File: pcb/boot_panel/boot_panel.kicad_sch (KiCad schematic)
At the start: 4 parts, among them J1 Conn_01x10_Socket

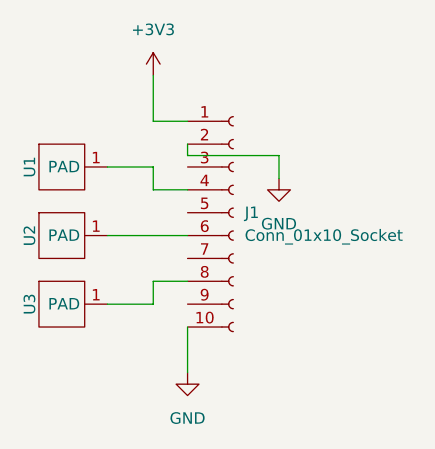
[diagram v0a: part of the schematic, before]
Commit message: move panel connector to fpc
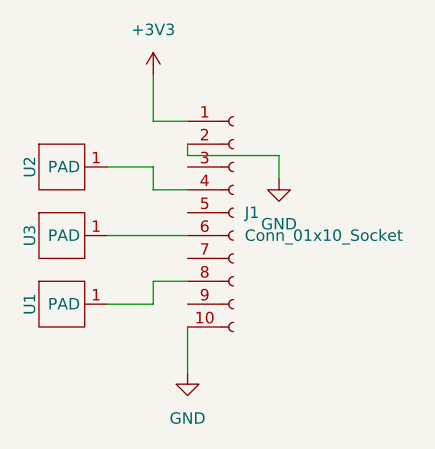
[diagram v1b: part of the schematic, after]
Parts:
- J1: footprint Connector_PinHeader_2.54mm:PinHeader_1x10_P2.54mm_Vertical_SMD_Pin1Left -> Connector_FFC-FPC:Hirose_FH12-10S-0.5SH_1x10-1MP_P0.50mm_Horizontal
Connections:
- net at U2.1 (PAD): now also J1.4 (Pin_4); no longer J1.6 (Pin_6)
- net at U1.1 (PAD): now also J1.8 (Pin_8); no longer J1.4 (Pin_4)
- net at U3.1 (PAD): now also J1.6 (Pin_6); no longer J1.8 (Pin_8)
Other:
- moved on the sheet: U1, U2, U3
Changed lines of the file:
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@@
 	(symbol
 		(lib_id "cap_pads:capacitive_pad")
-		(at 175.26 81.28 0)
+		(at 175.26 73.66 0)
 		(unit 1)
 		(exclude_from_sim no)
@@
 		(dnp no)
 		(property "Reference" "U2"
-			(at 171.704 85.09 90)
+			(at 171.704 77.47 90)
 			(effects
 				(font
@@
 		)
 		(property "Value" "~"
-			(at 175.26 81.28 0)
+			(at 175.26 73.66 0)
 			(effects
 				(font
@@
 		)
 		(property "Footprint" "cap_pads:square_20x20mm"
-			(at 175.26 81.28 0)
+			(at 175.26 73.66 0)
 			(effects
 				(font
@@
 		)
 		(property "Datasheet" ""
-			(at 175.26 81.28 0)
+			(at 175.26 73.66 0)
 			(effects
 				(font
@@
 		)
 		(property "Description" ""
-			(at 175.26 81.28 0)
+			(at 175.26 73.66 0)
 			(effects
 				(font
@@
 			)
 		)
-		(property "Footprint" "Connector_PinHeader_2.54mm:PinHeader_1x10_P2.54mm_Vertical_SMD_Pin1Left"
+		(property "Footprint" "Connector_FFC-FPC:Hirose_FH12-10S-0.5SH_1x10-1MP_P0.50mm_Horizontal"
 			(at 194.31 82.55 0)
 			(effects
@@
 	(symbol
 		(lib_id "cap_pads:capacitive_pad")
-		(at 175.26 88.9 0)
+		(at 175.26 81.28 0)
 		(unit 1)
 		(exclude_from_sim no)
@@
 		(dnp no)
 		(property "Reference" "U3"
-			(at 171.704 92.71 90)
+			(at 171.704 85.09 90)
 			(effects
 				(font
@@
 		)
 		(property "Value" "~"
-			(at 175.26 88.9 0)
+			(at 175.26 81.28 0)
 			(effects
 				(font
@@
 		)
 		(property "Footprint" "cap_pads:square_20x20mm"
-			(at 175.26 88.9 0)
+			(at 175.26 81.28 0)
 			(effects
 				(font
@@
 		)
 		(property "Datasheet" ""
-			(at 175.26 88.9 0)
+			(at 175.26 81.28 0)
 			(effects
 				(font
@@
 		)
 		(property "Description" ""
-			(at 175.26 88.9 0)
+			(at 175.26 81.28 0)
 			(effects
 				(font
@@
 	(symbol
 		(lib_id "cap_pads:capacitive_pad")
-		(at 175.26 73.66 0)
+		(at 175.26 88.9 0)
 		(unit 1)
 		(exclude_from_sim no)
@@
 		(dnp no)
 		(property "Reference" "U1"
-			(at 171.704 77.47 90)
+			(at 171.704 92.71 90)
 			(effects
 				(font
@@
 		)
 		(property "Value" "~"
-			(at 175.26 73.66 0)
+			(at 175.26 88.9 0)
 			(effects
 				(font
@@
 		)
 		(property "Footprint" "cap_pads:square_20x20mm"
-			(at 175.26 73.66 0)
+			(at 175.26 88.9 0)
 			(effects
 				(font
@@
 		)
 		(property "Datasheet" ""
-			(at 175.26 73.66 0)
+			(at 175.26 88.9 0)
 			(effects
 				(font
@@
 		)
 		(property "Description" ""
-			(at 175.26 73.66 0)
-			(effects
-				(font
+			(at 175.26 88.9 0)
+			(effects
+				(font

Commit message: MOre layout
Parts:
- added H1, H2, H3, H4: MountingHole, MountingHole:MountingHole_3.2mm_M3, symbol Mechanical:MountingHole

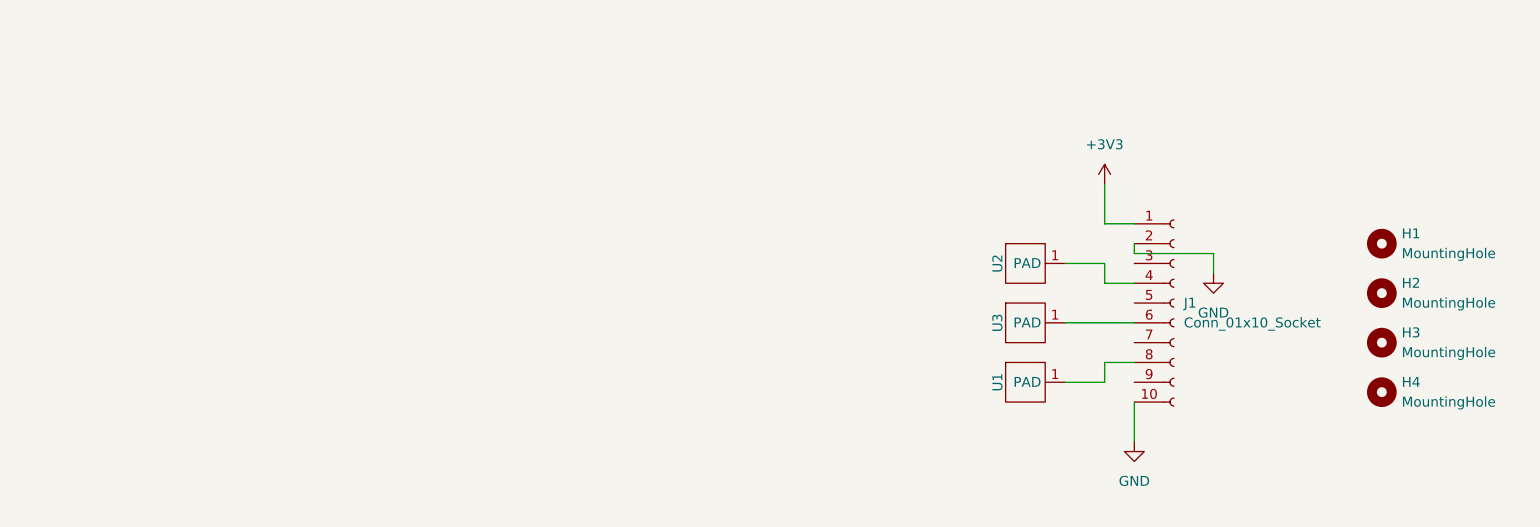
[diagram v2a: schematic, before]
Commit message: move cap sense ic to front panel
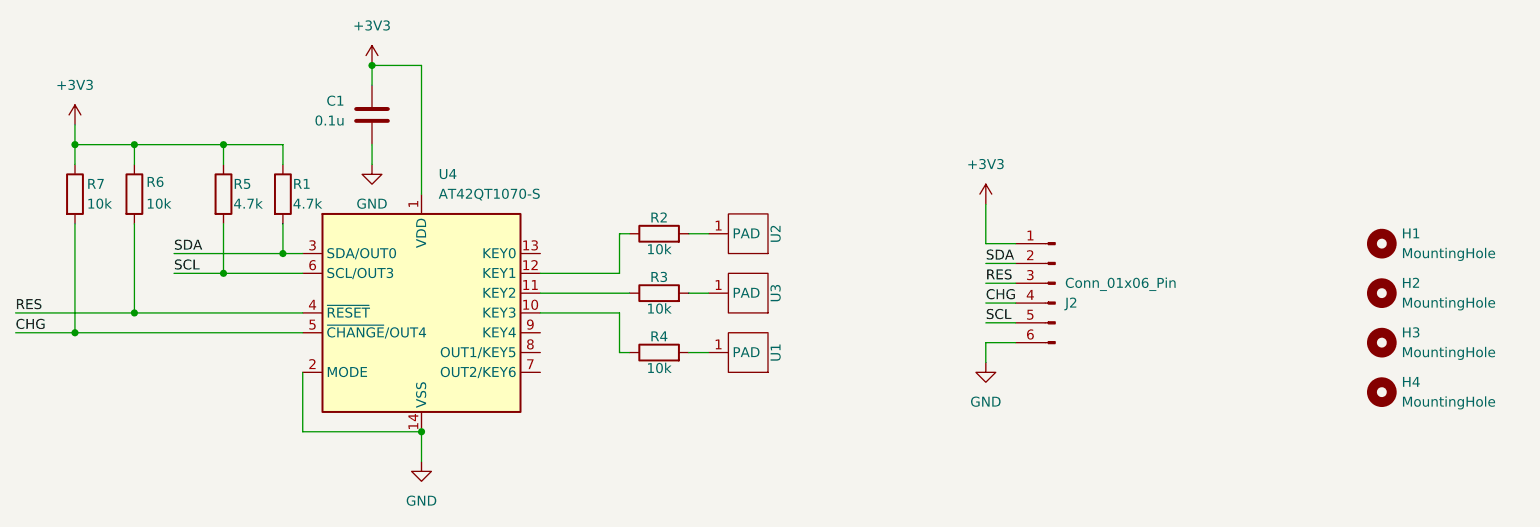
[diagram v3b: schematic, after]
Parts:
- removed J1: Conn_01x10_Socket, Connector_FFC-FPC:Hirose_FH12-10S-0.5SH_1x10-1MP_P0.50mm_Horizontal, symbol Connector:Conn_01x10_Socket
- added C1: 0.1u, Capacitor_SMD:C_0402_1005Metric, symbol Device:C
- added J2: Conn_01x06_Pin, Connector_FFC-FPC:Hirose_FH12-6S-0.5SH_1x06-1MP_P0.50mm_Horizontal, symbol Connector:Conn_01x06_Pin
- added R1, R5: 4.7k, Resistor_SMD:R_0402_1005Metric, symbol Device:R
- added R2, R3, R4, R6, R7: 10k, Resistor_SMD:R_0402_1005Metric, symbol Device:R
- added U4: AT42QT1070-S, Package_SO:SOIC-14_3.9x8.7mm_P1.27mm, symbol Sensor_Touch:AT42QT1070-S
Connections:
- net +3V3: now also C1.1, J2.1 (Pin_1), R1.1, R5.1, R6.1, R7.1, U4.1 (VDD)
- net GND: now also C1.2, J2.6 (Pin_6), U4.14 (VSS), U4.2 (MODE)
- net at U2.1 (PAD): now also R2.2
- net at U3.1 (PAD): now also R3.2
- net at U1.1 (PAD): now also R4.2
- new net: R4.1, U4.10 (KEY3)
- new net: R3.1, U4.11 (KEY2)
- new net: R2.1, U4.12 (KEY1)
- new net CHG: J2.4 (Pin_4), R7.2, U4.5 (~{CHANGE}/OUT4)
- new net RES: J2.3 (Pin_3), R6.2, U4.4 (~{RESET})
- new net SCL: J2.5 (Pin_5), R5.2, U4.6 (SCL/OUT3)
- new net SDA: J2.2 (Pin_2), R1.2, U4.3 (SDA/OUT0)
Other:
- moved on the sheet: U1, U2, U3

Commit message: More layout
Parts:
- C1: footprint Capacitor_SMD:C_0402_1005Metric -> Capacitor_SMD:C_0603_1608Metric_Pad1.08x0.95mm_HandSolder
- R1, R2, R3, R4, R5, R6, R7: footprint Resistor_SMD:R_0402_1005Metric -> Resistor_SMD:R_0603_1608Metric_Pad0.98x0.95mm_HandSolder
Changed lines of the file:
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@@
 			)
 		)
-		(property "Footprint" "Capacitor_SMD:C_0402_1005Metric"
+		(property "Footprint" "Capacitor_SMD:C_0603_1608Metric_Pad1.08x0.95mm_HandSolder"
 			(at 92.4052 62.23 0)
 			(effects
@@
 			)
 		)
-		(property "Footprint" "Resistor_SMD:R_0402_1005Metric"
+		(property "Footprint" "Resistor_SMD:R_0603_1608Metric_Pad0.98x0.95mm_HandSolder"
 			(at 51.562 68.58 90)
 			(effects
@@
 			)
 		)
-		(property "Footprint" "Resistor_SMD:R_0402_1005Metric"
+		(property "Footprint" "Resistor_SMD:R_0603_1608Metric_Pad0.98x0.95mm_HandSolder"
 			(at 70.612 68.58 90)
 			(effects
@@
 			)
 		)
-		(property "Footprint" "Resistor_SMD:R_0402_1005Metric"
+		(property "Footprint" "Resistor_SMD:R_0603_1608Metric_Pad0.98x0.95mm_HandSolder"
 			(at 128.27 90.678 90)
 			(effects
@@
 			)
 		)
-		(property "Footprint" "Resistor_SMD:R_0402_1005Metric"
+		(property "Footprint" "Resistor_SMD:R_0603_1608Metric_Pad0.98x0.95mm_HandSolder"
 			(at 128.27 75.438 90)
 			(effects
@@
 			)
 		)
-		(property "Footprint" "Resistor_SMD:R_0402_1005Metric"
+		(property "Footprint" "Resistor_SMD:R_0603_1608Metric_Pad0.98x0.95mm_HandSolder"
 			(at 59.182 68.58 90)
 			(effects
@@
 			)
 		)
-		(property "Footprint" "Resistor_SMD:R_0402_1005Metric"
+		(property "Footprint" "Resistor_SMD:R_0603_1608Metric_Pad0.98x0.95mm_HandSolder"
 			(at 78.232 68.58 90)
 			(effects
@@
 			)
 		)
-		(property "Footprint" "Resistor_SMD:R_0402_1005Metric"
+		(property "Footprint" "Resistor_SMD:R_0603_1608Metric_Pad0.98x0.95mm_HandSolder"
 			(at 128.27 83.058 90)
 			(effects
